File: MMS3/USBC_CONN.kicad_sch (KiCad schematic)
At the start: 5 parts, among them J800 USB_C_Receptacle_USB2.0_16P, U401 TPD2EUSB30DRTR-TP

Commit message: backup commit
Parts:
- removed C800: 100nF, PCM_JLCPCB:C_0402, symbol PCM_JLCPCB-Capacitors:0402,100nF,(2)
- added C801: 100nF, PCM_JLCPCB:C_0402, symbol PCM_JLCPCB-Capacitors:0402,100nF,(2)
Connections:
- net GND: now also C801.2
- net VBUS: now also C801.1
- net CC1: no longer names the net of J800.A5 (CC1)
- net CC2: no longer names the net of J800.B5 (CC2)
- no-connect marks 2 -> 4

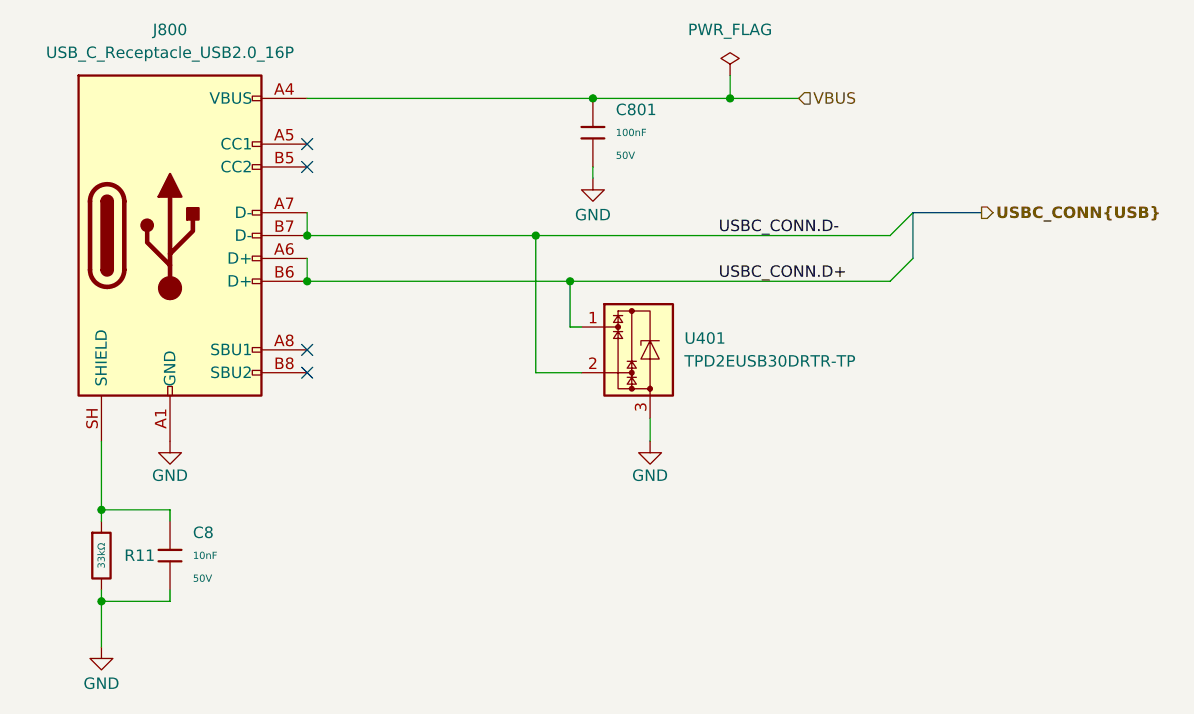
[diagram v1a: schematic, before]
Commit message: updated schematic, removed annotation
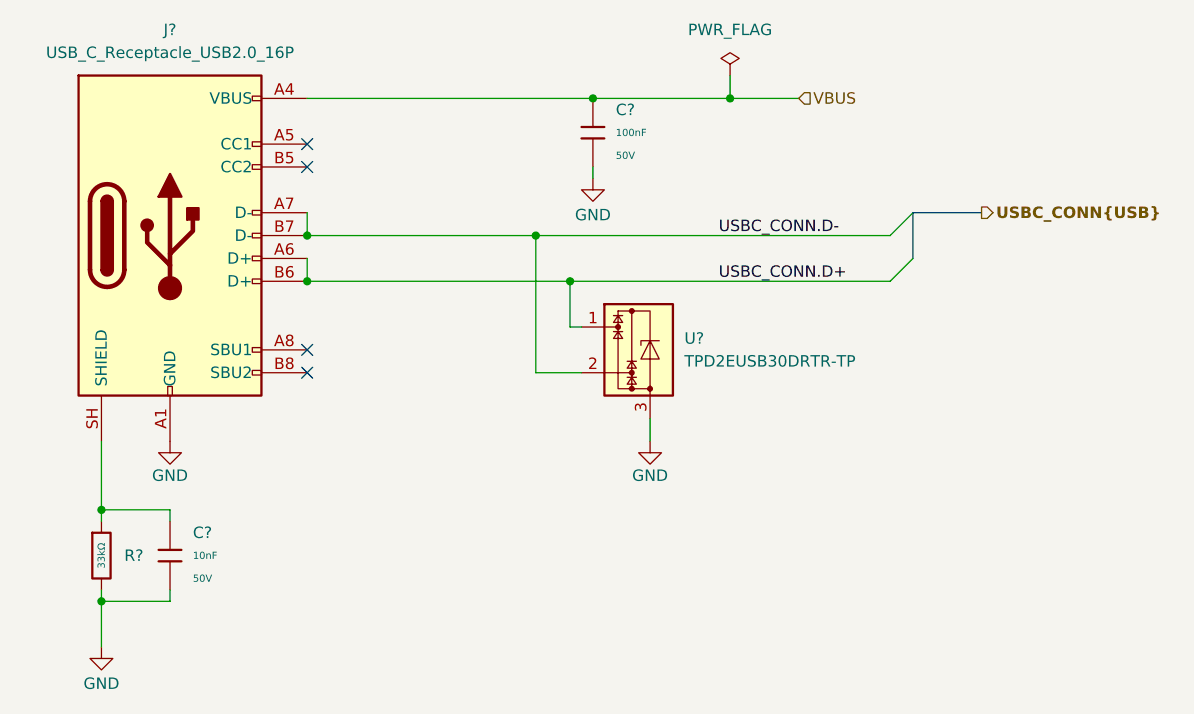
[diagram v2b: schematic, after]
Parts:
- renumbered C8 to C?, C801 to C?, J800 to J?, R11 to R?, U401 to U?
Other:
- title: MMS3 -> MMS3 CH32L103 Version
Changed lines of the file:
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@@
 	(paper "A4")
 	(title_block
-		(title "MMS3")
-		(date "2026-04-03")
+		(title "MMS3 CH32L103 Version")
+		(date "2026-05-18")
 		(rev "XA1")
 		(company "(c) Modular Mechanica")
-		(comment 1 "Artem Horiunov")
-		(comment 2 "DESIGNED IN POLAND")
+		(comment 1 "DESIGNED IN POLAND")
+		(comment 2 "Forked by: Wojciech Szafranski")
+		(comment 3 "Made by: Artem Horiunov")
 	)
 	(junction
@@
 		(in_pos_files yes)
 		(dnp no)
-		(property "Reference" "#PWR0801"
+		(property "Reference" "#PWR?"
 			(at 147.32 88.9 0)
 			(hide yes)
@@
 			(project "MMS3"
 				(path "/712cea22-140d-4c92-923f-f4998caf3ecd/74791e0a-96ec-438a-97e0-aa99273ef224"
-					(reference "#PWR0801")
+					(reference "#PWR?")
 					(unit 1)
 				)
@@
 		(in_pos_files yes)
 		(dnp no)
-		(property "Reference" "#PWR0808"
+		(property "Reference" "#PWR?"
 			(at 92.71 140.97 0)
 			(hide yes)
@@
 			(project "MMS3"
 				(path "/712cea22-140d-4c92-923f-f4998caf3ecd/74791e0a-96ec-438a-97e0-aa99273ef224"
-					(reference "#PWR0808")
+					(reference "#PWR?")
 					(unit 1)
 				)
@@
 		(in_pos_files yes)
 		(dnp no)
-		(property "Reference" "#PWR0802"
+		(property "Reference" "#PWR?"
 			(at 153.67 118.11 0)
 			(hide yes)
@@
 			(project "MMS3"
 				(path "/712cea22-140d-4c92-923f-f4998caf3ecd/74791e0a-96ec-438a-97e0-aa99273ef224"
-					(reference "#PWR0802")
+					(reference "#PWR?")
 					(unit 1)
 				)
@@
 		(dnp no)
 		(fields_autoplaced yes)
-		(property "Reference" "#FLG03"
+		(property "Reference" "#FLG?"
 			(at 162.56 69.215 0)
 			(hide yes)
@@
 			(project "MMS3"
 				(path "/712cea22-140d-4c92-923f-f4998caf3ecd/74791e0a-96ec-438a-97e0-aa99273ef224"
-					(reference "#FLG03")
+					(reference "#FLG?")
 					(unit 1)
 				)
@@
 		(dnp no)
 		(fields_autoplaced yes)
-		(property "Reference" "J800"
+		(property "Reference" "J?"
 			(at 100.33 66.04 0)
 			(show_name no)
@@
 			(project "MMS3"
 				(path "/712cea22-140d-4c92-923f-f4998caf3ecd/74791e0a-96ec-438a-97e0-aa99273ef224"
-					(reference "J800")
+					(reference "J?")
 					(unit 1)
 				)
@@
 		(dnp no)
 		(fields_autoplaced yes)
-		(property "Reference" "C8"
+		(property "Reference" "C?"
 			(at 102.87 121.9199 0)
 			(show_name no)
@@
 			(project "MMS3"
 				(path "/712cea22-140d-4c92-923f-f4998caf3ecd/74791e0a-96ec-438a-97e0-aa99273ef224"
-					(reference "C8")
+					(reference "C?")
 					(unit 1)
 				)
@@
 		(dnp no)
 		(fields_autoplaced yes)
-		(property "Reference" "U401"
+		(property "Reference" "U?"
 			(at 157.48 100.3299 0)
 			(show_name no)
@@
 			(project "MMS3"
 				(path "/712cea22-140d-4c92-923f-f4998caf3ecd/74791e0a-96ec-438a-97e0-aa99273ef224"
-					(reference "U401")
+					(reference "U?")
 					(unit 1)
 				)
@@
 		(dnp no)
 		(fields_autoplaced yes)
-		(property "Reference" "C801"
+		(property "Reference" "C?"
 			(at 149.86 74.9299 0)
 			(show_name no)
@@
 			(project "MMS3"
 				(path "/712cea22-140d-4c92-923f-f4998caf3ecd/74791e0a-96ec-438a-97e0-aa99273ef224"
-					(reference "C801")
+					(reference "C?")
 					(unit 1)
 				)
@@
 		(in_pos_files yes)
 		(dnp no)
-		(property "Reference" "#PWR0804"
+		(property "Reference" "#PWR?"
 			(at 100.33 118.11 0)
 			(hide yes)
@@
 			(project "MMS3"
 				(path "/712cea22-140d-4c92-923f-f4998caf3ecd/74791e0a-96ec-438a-97e0-aa99273ef224"
-					(reference "#PWR0804")
+					(reference "#PWR?")
 					(unit 1)
 				)
@@
 		(dnp no)
 		(fields_autoplaced yes)
-		(property "Reference" "R11"
+		(property "Reference" "R?"
 			(at 95.25 124.4599 0)
 			(show_name no)
@@
 			(project "MMS3"
 				(path "/712cea22-140d-4c92-923f-f4998caf3ecd/74791e0a-96ec-438a-97e0-aa99273ef224"
-					(reference "R11")
+					(reference "R?")
 					(unit 1)
 				)

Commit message: initial PCB update
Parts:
- gave numbers to parts that had none: 5
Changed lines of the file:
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@@
 		(in_pos_files yes)
 		(dnp no)
-		(property "Reference" "#PWR?"
+		(property "Reference" "#PWR080"
 			(at 147.32 88.9 0)
 			(hide yes)
@@
 			(project "MMS3"
 				(path "/712cea22-140d-4c92-923f-f4998caf3ecd/74791e0a-96ec-438a-97e0-aa99273ef224"
-					(reference "#PWR?")
+					(reference "#PWR080")
 					(unit 1)
 				)
@@
 		(in_pos_files yes)
 		(dnp no)
-		(property "Reference" "#PWR?"
+		(property "Reference" "#PWR078"
 			(at 92.71 140.97 0)
 			(hide yes)
@@
 			(project "MMS3"
 				(path "/712cea22-140d-4c92-923f-f4998caf3ecd/74791e0a-96ec-438a-97e0-aa99273ef224"
-					(reference "#PWR?")
+					(reference "#PWR078")
 					(unit 1)
 				)
@@
 		(in_pos_files yes)
 		(dnp no)
-		(property "Reference" "#PWR?"
+		(property "Reference" "#PWR081"
 			(at 153.67 118.11 0)
 			(hide yes)
@@
 			(project "MMS3"
 				(path "/712cea22-140d-4c92-923f-f4998caf3ecd/74791e0a-96ec-438a-97e0-aa99273ef224"
-					(reference "#PWR?")
+					(reference "#PWR081")
 					(unit 1)
 				)
@@
 		(dnp no)
 		(fields_autoplaced yes)
-		(property "Reference" "#FLG?"
+		(property "Reference" "#FLG02"
 			(at 162.56 69.215 0)
 			(hide yes)
@@
 			(project "MMS3"
 				(path "/712cea22-140d-4c92-923f-f4998caf3ecd/74791e0a-96ec-438a-97e0-aa99273ef224"
-					(reference "#FLG?")
+					(reference "#FLG02")
 					(unit 1)
 				)
@@
 		(dnp no)
 		(fields_autoplaced yes)
-		(property "Reference" "J?"
+		(property "Reference" "J4"
 			(at 100.33 66.04 0)
 			(show_name no)
@@
 			(project "MMS3"
 				(path "/712cea22-140d-4c92-923f-f4998caf3ecd/74791e0a-96ec-438a-97e0-aa99273ef224"
-					(reference "J?")
+					(reference "J4")
 					(unit 1)
 				)
@@
 		(dnp no)
 		(fields_autoplaced yes)
-		(property "Reference" "C?"
+		(property "Reference" "C14"
 			(at 102.87 121.9199 0)
 			(show_name no)
@@
 			(project "MMS3"
 				(path "/712cea22-140d-4c92-923f-f4998caf3ecd/74791e0a-96ec-438a-97e0-aa99273ef224"
-					(reference "C?")
+					(reference "C14")
 					(unit 1)
 				)
@@
 		(dnp no)
 		(fields_autoplaced yes)
-		(property "Reference" "U?"
+		(property "Reference" "U3"
 			(at 157.48 100.3299 0)
 			(show_name no)
@@
 			(project "MMS3"
 				(path "/712cea22-140d-4c92-923f-f4998caf3ecd/74791e0a-96ec-438a-97e0-aa99273ef224"
-					(reference "U?")
+					(reference "U3")
 					(unit 1)
 				)
@@
 		(dnp no)
 		(fields_autoplaced yes)
-		(property "Reference" "C?"
+		(property "Reference" "C15"
 			(at 149.86 74.9299 0)
 			(show_name no)
@@
 			(project "MMS3"
 				(path "/712cea22-140d-4c92-923f-f4998caf3ecd/74791e0a-96ec-438a-97e0-aa99273ef224"
-					(reference "C?")
+					(reference "C15")
 					(unit 1)
 				)
@@
 		(in_pos_files yes)
 		(dnp no)
-		(property "Reference" "#PWR?"
+		(property "Reference" "#PWR079"
 			(at 100.33 118.11 0)
 			(hide yes)
@@
 			(project "MMS3"
 				(path "/712cea22-140d-4c92-923f-f4998caf3ecd/74791e0a-96ec-438a-97e0-aa99273ef224"
-					(reference "#PWR?")
+					(reference "#PWR079")
 					(unit 1)
 				)
@@
 		(dnp no)
 		(fields_autoplaced yes)
-		(property "Reference" "R?"
+		(property "Reference" "R14"
 			(at 95.25 124.4599 0)
 			(show_name no)
@@
 			(project "MMS3"
 				(path "/712cea22-140d-4c92-923f-f4998caf3ecd/74791e0a-96ec-438a-97e0-aa99273ef224"
-					(reference "R?")
+					(reference "R14")
 					(unit 1)
 				)
